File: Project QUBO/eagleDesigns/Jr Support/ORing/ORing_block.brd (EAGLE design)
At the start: 152.4 x 101.6 mm, 87 parts

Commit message: 
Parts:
- moved U$15 268.1 mm to (38.9, 88.2), turned to 270 degrees
- moved U$14 260.7 mm to (13.8, 83.4)
- moved U$5 256.3 mm to (22.3, 87.3), turned to 180 degrees
- moved R38 253.3 mm to (21.9, 84.6)
- moved R37 251.2 mm to (21.9, 82.3)
- moved C3 251.2 mm to (27.3, 82.7), turned to 90 degrees
- moved BATT1_IN 228.9 mm to (20.6, 94.5)
- moved U$20 198.5 mm to (88.5, 87.7), turned to 270 degrees
- moved U$19 180.4 mm to (60.8, 83.8)
- moved R35 174.2 mm to (75.5, 87.2), turned to 180 degrees
- moved R33 174.1 mm to (101.1, 129.5)
- moved C20 173.5 mm to (75.7, 83.5)
- moved U$13 171.6 mm to (70.0, 87.2), turned to 180 degrees
- moved LED7 171.4 mm to (98.2, 133.7), turned to 180 degrees
- moved R36 171.3 mm to (69.9, 84.3)
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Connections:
- removed net GND1: LED8.P$2
- removed net V_BATT3: R34.2
- net GND: now also LED8.P$2
- net V_BATT1: now also R34.2
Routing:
- net GND: track 15.0 -> 80.2 mm
- net V_BATT2: track 0.00 -> 61.6 mm, vias 0 -> 2
- net V_BATT: track 15.4 -> 51.1 mm, vias 0 -> 2
- net N$10: track 0.00 -> 31.5 mm, vias 0 -> 2
- net N$8: track 0.00 -> 30.6 mm, vias 0 -> 2
- net N$36: track 0.00 -> 24.5 mm
- net N$35: track 0.00 -> 23.9 mm
- net N$1: track 0.00 -> 23.3 mm, vias 0 -> 2
- net N$41: track 0.00 -> 23.0 mm, vias 0 -> 2
- net N$38: track 0.00 -> 20.2 mm
- net N$45: track 0.00 -> 20.2 mm
- net N$40: track 0.00 -> 20.0 mm
- net N$28: track 0.00 -> 18.9 mm, vias 0 -> 2
- net N$15: track 0.00 -> 17.8 mm
- net N$3: track 0.00 -> 13.2 mm
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- added copper zone on layer 1, net N$38

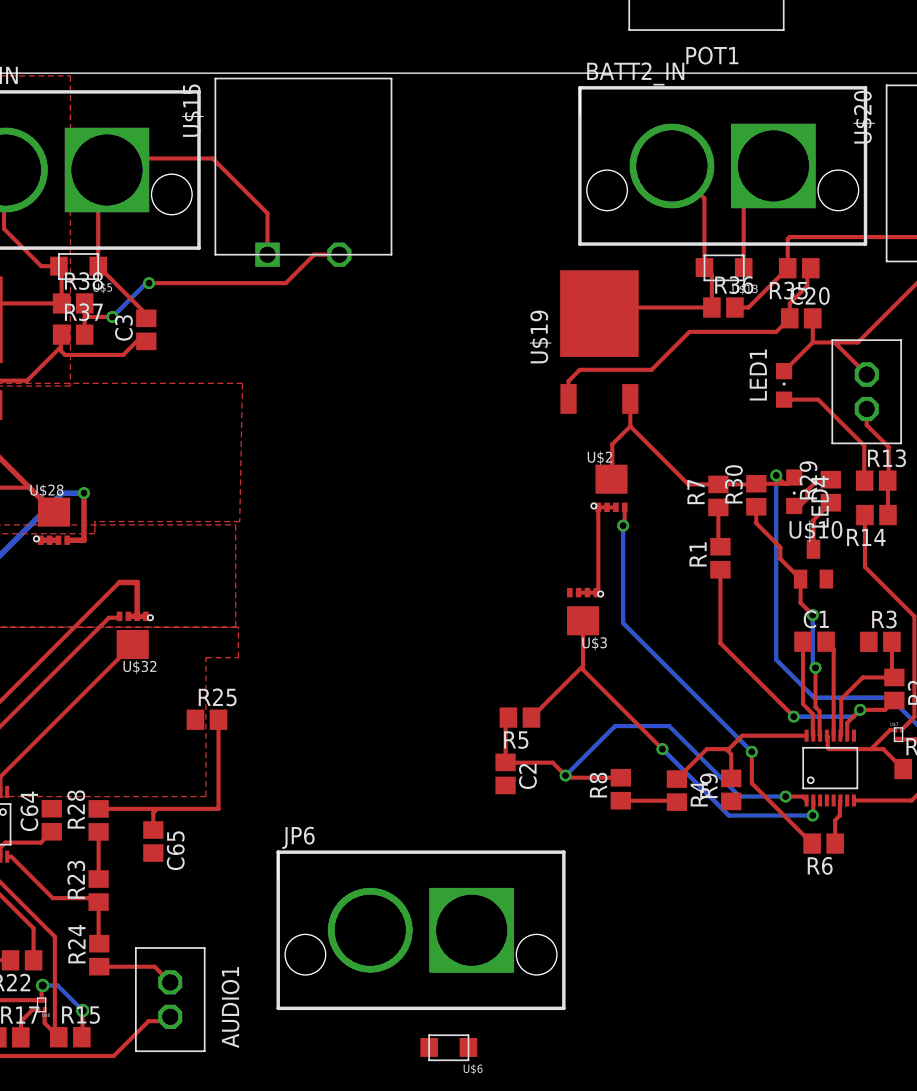
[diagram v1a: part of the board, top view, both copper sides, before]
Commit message: 
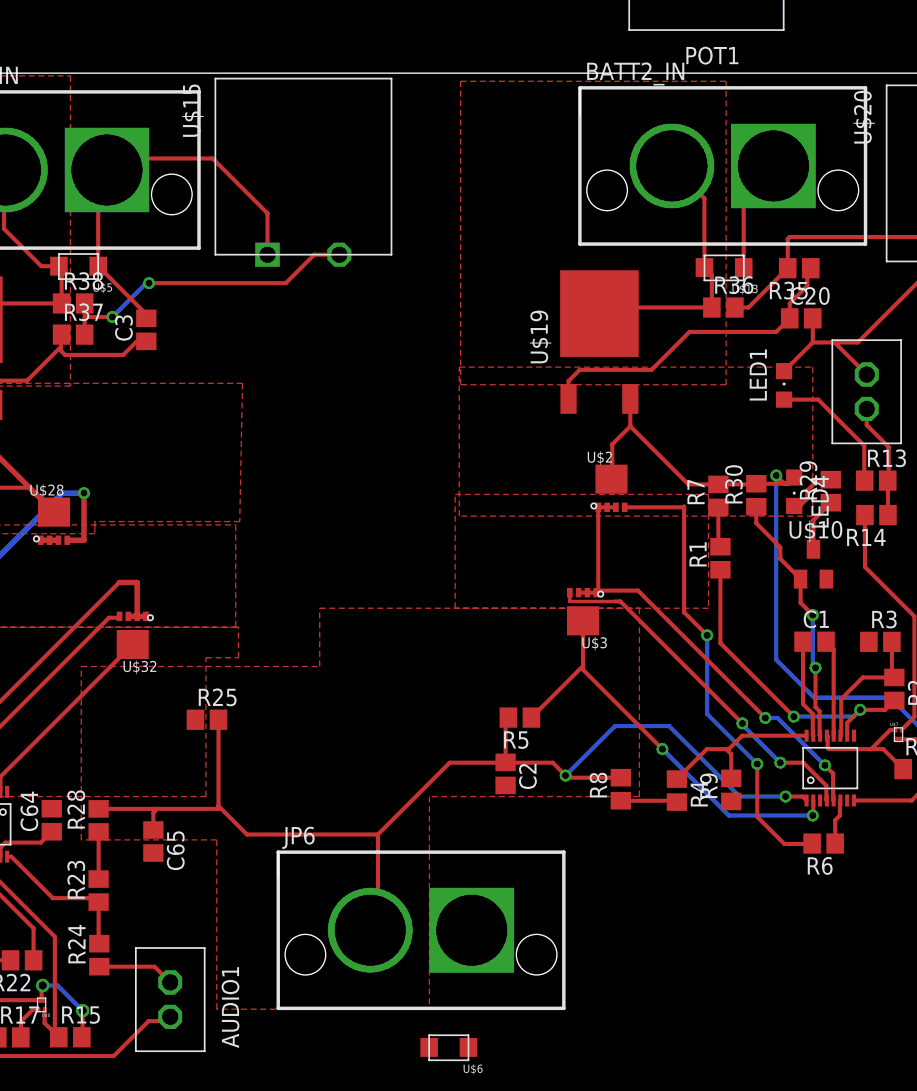
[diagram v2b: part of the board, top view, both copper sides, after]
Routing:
- net V_BATT: track 51.1 -> 82.6 mm
- net N$11: track 0.00 -> 26.4 mm, vias 0 -> 2
- net N$9: track 8.96 -> 33.9 mm, vias 0 -> 2
- net N$8: track 30.6 -> 34.4 mm
- added copper zone on layer 1, net N$45
- added copper zone on layer 1, net N$9
- added copper zone on layer 1, net V_BATT
- added copper zone on layer 1, net V_BATT2
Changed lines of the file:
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@@
 <contactref element="JP6" pad="P$1"/>
 <contactref element="U$6" pad="P$2"/>
-<wire x1="32.63" y1="53.87" x2="32.63" y2="47.29" width="0.3048" layer="1"/>
+<wire x1="32.63" y1="47.5" x2="32.63" y2="53.87" width="0.3048" layer="1"/>
+<wire x1="32.63" y1="47.5" x2="32.63" y2="47.29" width="0.3048" layer="1"/>
 <wire x1="28.1" y1="47.29" x2="32.63" y2="47.29" width="0.3048" layer="1"/>
 <wire x1="28.1" y1="47.29" x2="23.78" y2="47.29" width="0.3048" layer="1"/>
@@
 <wire x1="61.9" y1="53.4" x2="58.25" y2="49.75" width="0.3048" layer="16"/>
 <via x="58.25" y="49.75" extent="1-16" drill="0.5"/>
-<wire x1="43.8335" y1="38.33" x2="53.84" y2="50.7" width="0" layer="19" extent="1-1"/>
-<wire x1="48.18" y1="29.68" x2="43.8335" y2="38.33" width="0" layer="19" extent="1-1"/>
-<wire x1="32.63" y1="47.29" x2="43.8335" y2="38.33" width="0" layer="19" extent="1-1"/>
+<wire x1="53.84" y1="50.7" x2="49.7" y2="50.7" width="0.3048" layer="1"/>
+<wire x1="49.7" y1="50.7" x2="44.4" y2="45.4" width="0.3048" layer="1"/>
+<wire x1="44.4" y1="45.4" x2="44.4" y2="38.8965" width="0.3048" layer="1"/>
+<wire x1="44.4" y1="38.8965" x2="43.8335" y2="38.33" width="0.3048" layer="1"/>
+<wire x1="44.4" y1="45.4" x2="34.73" y2="45.4" width="0.3048" layer="1"/>
+<wire x1="34.73" y1="45.4" x2="32.63" y2="47.5" width="0.3048" layer="1"/>
+<polygon width="0.3048" layer="1" rank="4">
+<vertex x="31.7" y="57.8"/>
+<vertex x="40.1" y="57.8"/>
+<vertex x="40.1" y="62.1"/>
+<vertex x="63.7" y="62.1"/>
+<vertex x="63.7" y="48.2"/>
+<vertex x="48.2" y="48.2"/>
+<vertex x="48.2" y="32.5"/>
+<vertex x="32.5" y="32.5"/>
+<vertex x="32.5" y="45"/>
+<vertex x="22.5" y="45"/>
+<vertex x="22.5" y="57.8"/>
+</polygon>
+<wire x1="43.8335" y1="38.33" x2="48.18" y2="29.68" width="0" layer="19" extent="1-1"/>
 <wire x1="17.03" y1="48.54" x2="23.78" y2="47.29" width="0" layer="19" extent="1-1"/>
 </signal>
@@
 <contactref element="R6" pad="2"/>
 <contactref element="U$2" pad="GATE"/>
-<wire x1="76.45" y1="44.73" x2="72" y2="49.18" width="0.3048" layer="1"/>
-<wire x1="72" y1="49.18" x2="72" y2="51.5" width="0.3048" layer="1"/>
-<via x="72" y="51.5" extent="1-16" drill="0.5"/>
-<wire x1="72" y1="51.5" x2="62.5" y2="61" width="0.3048" layer="16"/>
-<wire x1="62.5" y1="61" x2="62.5" y2="68.2" width="0.3048" layer="16"/>
-<via x="62.5" y="68.2" extent="1-16" drill="0.5"/>
-<wire x1="62.5" y1="68.2" x2="62.615" y2="68.315" width="0.3048" layer="1"/>
-<wire x1="62.615" y1="68.315" x2="62.615" y2="69.55" width="0.3048" layer="1"/>
+<wire x1="62.615" y1="69.55" x2="66.95" y2="69.55" width="0.3048" layer="1"/>
+<wire x1="66.95" y1="69.55" x2="67" y2="69.6" width="0.3048" layer="1"/>
+<wire x1="67" y1="69.6" x2="67" y2="61.8" width="0.3048" layer="1"/>
+<wire x1="67" y1="61.8" x2="68.7" y2="60.1" width="0.3048" layer="1"/>
+<via x="68.7" y="60.1" extent="1-16" drill="0.5"/>
+<wire x1="68.7" y1="60.1" x2="68.7" y2="54.3" width="0.3048" layer="16"/>
+<wire x1="68.7" y1="54.3" x2="72.4" y2="50.6" width="0.3048" layer="16"/>
+<via x="72.4" y="50.6" extent="1-16" drill="0.5"/>
+<wire x1="72.4" y1="50.6" x2="72.4" y2="46.7" width="0.3048" layer="1"/>
+<wire x1="72.4" y1="46.7" x2="74.4" y2="44.7" width="0.3048" layer="1"/>
+<wire x1="74.4" y1="44.7" x2="76.42" y2="44.7" width="0.3048" layer="1"/>
+<wire x1="76.42" y1="44.7" x2="76.45" y2="44.73" width="0.3048" layer="1"/>
 </signal>
 <signal name="N$9">
@@
 <wire x1="59.865" y1="63.25" x2="60.515" y2="63.25" width="0.3048" layer="1"/>
 <wire x1="59.215" y1="63.25" x2="59.865" y2="63.25" width="0.3048" layer="1"/>
-<wire x1="60.665" y1="63.4" x2="78.04" y2="47.91" width="0" layer="19" extent="1-1"/>
+<wire x1="60.665" y1="63.4" x2="63.6" y2="63.4" width="0.3048" layer="1"/>
+<wire x1="63.6" y1="63.4" x2="73" y2="54" width="0.3048" layer="1"/>
+<via x="73" y="54" extent="1-16" drill="0.5"/>
+<wire x1="73" y1="54" x2="73.9" y2="54" width="0.3048" layer="16"/>
+<wire x1="73.9" y1="54" x2="77.4" y2="50.5" width="0.3048" layer="16"/>
+<via x="77.4" y="50.5" extent="1-16" drill="0.5"/>
+<wire x1="77.4" y1="50.5" x2="78" y2="49.9" width="0.3048" layer="1"/>
+<wire x1="78" y1="49.9" x2="78" y2="47.95" width="0.3048" layer="1"/>
+<wire x1="78" y1="47.95" x2="78.04" y2="47.91" width="0.3048" layer="1"/>
+<polygon width="0.3048" layer="1">
+<vertex x="50.1" y="70.5"/>
+<vertex x="68.8" y="70.5"/>
+<vertex x="68.8" y="62.1"/>
+<vertex x="50.1" y="62.1"/>
+</polygon>
 </signal>
 <signal name="N$10">
@@
 <contactref element="U$1" pad="DGATE"/>
 <contactref element="U$3" pad="GATE"/>
-<wire x1="58.565" y1="63.25" x2="77.54" y2="47.91" width="0" layer="19" extent="1-1"/>
+<wire x1="58.565" y1="63.25" x2="58.565" y2="62.6" width="0.254" layer="1"/>
+<wire x1="58.565" y1="62.6" x2="61.9" y2="62.6" width="0.254" layer="1"/>
+<wire x1="61.9" y1="62.6" x2="62.3" y2="62.6" width="0.3048" layer="1"/>
+<wire x1="62.3" y1="62.6" x2="71.3" y2="53.6" width="0.3048" layer="1"/>
+<via x="71.3" y="53.6" extent="1-16" drill="0.5"/>
+<wire x1="71.3" y1="53.6" x2="71.3" y2="53.5" width="0.3048" layer="16"/>
+<wire x1="71.3" y1="53.5" x2="74.1" y2="50.7" width="0.3048" layer="16"/>
+<via x="74.1" y="50.7" extent="1-16" drill="0.5"/>
+<wire x1="74.1" y1="50.7" x2="75.8" y2="50.7" width="0.3048" layer="1"/>
+<wire x1="75.8" y1="50.7" x2="77.5" y2="49" width="0.3048" layer="1"/>
+<wire x1="77.5" y1="49" x2="77.5" y2="47.95" width="0.3048" layer="1"/>
+<wire x1="77.5" y1="47.95" x2="77.54" y2="47.91" width="0.3048" layer="1"/>
 </signal>
 <signal name="V_BATT2">
@@
 <wire x1="85.3" y1="52" x2="84.9" y2="51.6" width="0.3048" layer="1"/>
 <wire x1="76.6" y1="55.5" x2="82.2" y2="55.5" width="0.3048" layer="16"/>
+<polygon width="0.3048" layer="1" rank="2">
+<vertex x="50.4" y="79.9"/>
+<vertex x="76.5" y="79.9"/>
+<vertex x="76.5" y="68.9"/>
+<vertex x="50.4" y="68.9"/>
+</polygon>
 <wire x1="105.23" y1="123.94" x2="101.95" y2="129.5" width="0" layer="19" extent="1-1"/>
 <wire x1="95.9" y1="126.82" x2="101.95" y2="129.5" width="0" layer="19" extent="1-1"/>
@@
 <wire x1="69.05" y1="84.3" x2="61.2" y2="84.3" width="0.3048" layer="1"/>
 <wire x1="61.2" y1="84.3" x2="60.75" y2="83.85" width="0.3048" layer="1"/>
+<polygon width="0.3048" layer="1">
+<vertex x="50.5" y="101"/>
+<vertex x="70.1" y="101"/>
+<vertex x="70.1" y="78.6"/>
+<vertex x="50.5" y="78.6"/>
+</polygon>
 </signal>
 <signal name="N$35">

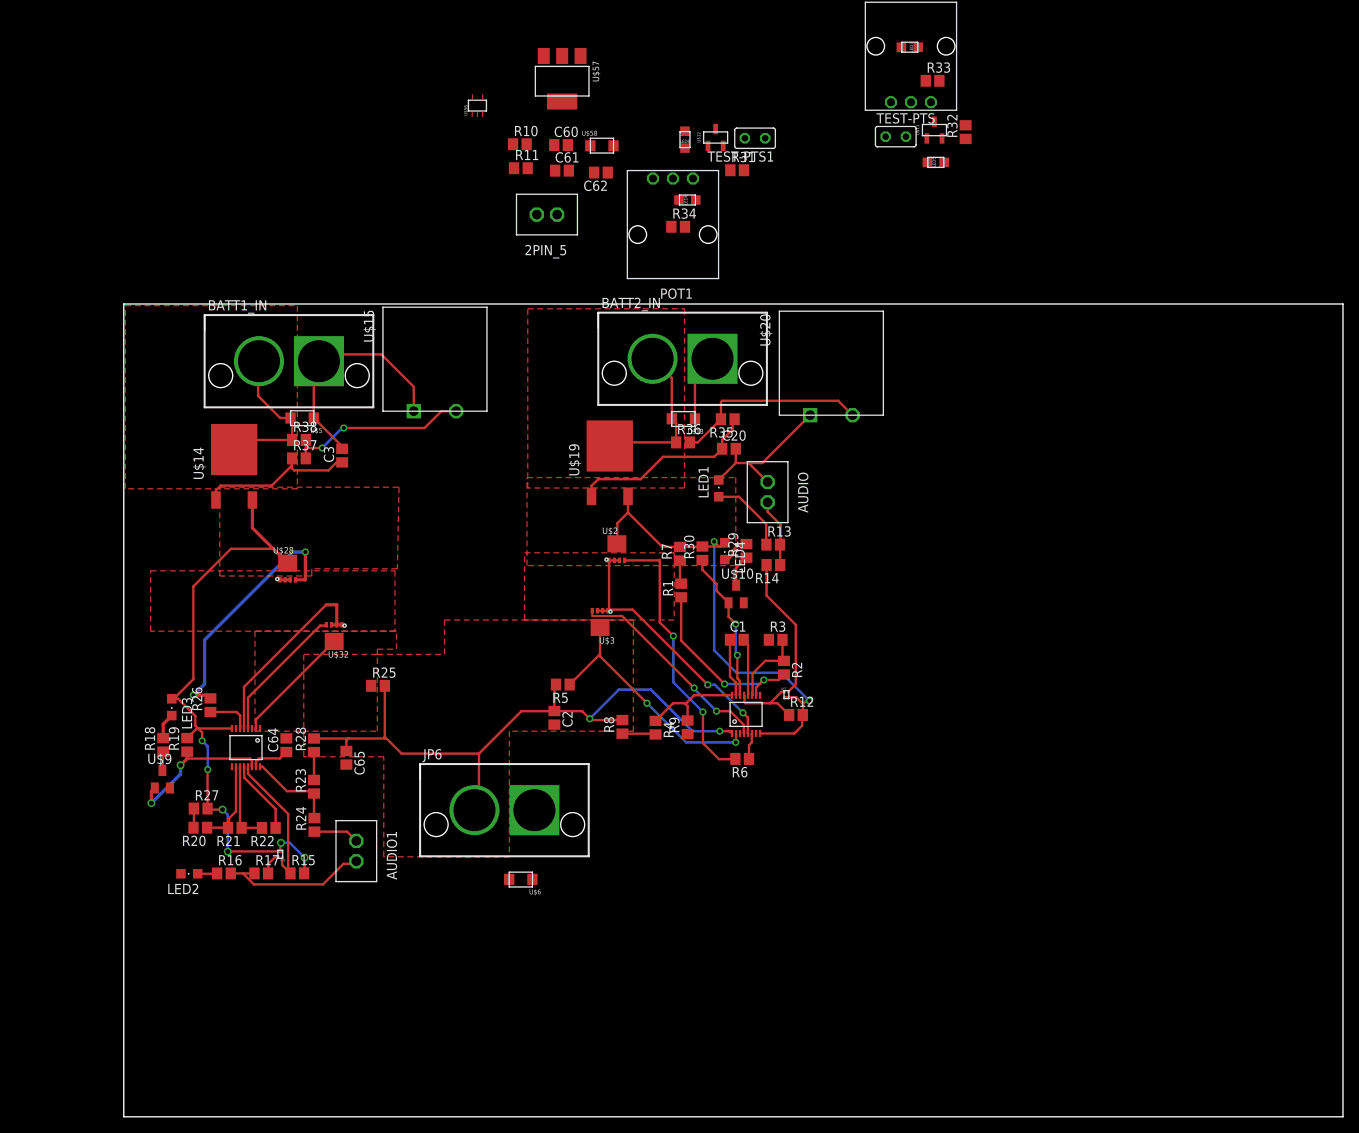
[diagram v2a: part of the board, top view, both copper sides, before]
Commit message: 
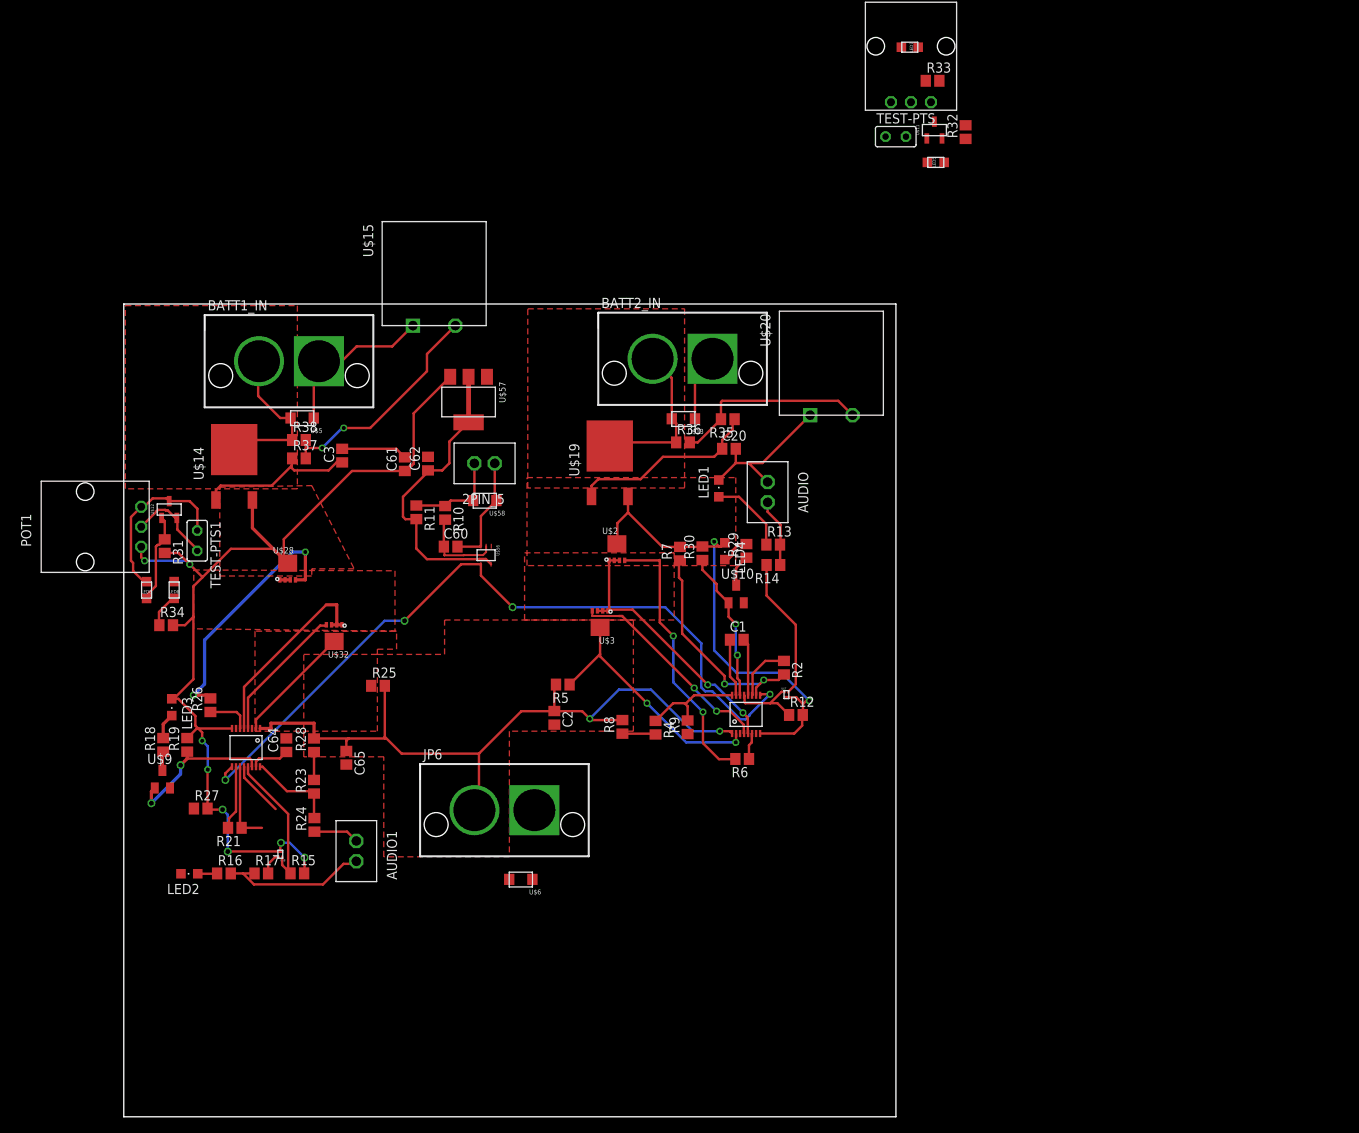
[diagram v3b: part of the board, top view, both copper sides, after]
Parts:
- removed R1, R20, R22, R3: 10k, resistor:R0805
- R2: value 12k -> 20.8k
- moved LED6 87.7 mm to (2.85, 65.8)
- moved TEST-PTS1 86.0 mm to (9.18, 72.0), turned to 270 degrees
- moved R31 85.6 mm to (5.12, 71.3), turned to 270 degrees
- moved U$12 82.6 mm to (5.68, 75.9)
- moved R34 81.1 mm to (5.30, 61.5)
- moved LED8 80.6 mm to (6.30, 65.8), turned to 90 degrees
- moved POT1 79.5 mm to (2.18, 73.8), turned to 90 degrees
- moved U$56 56.2 mm to (45.3, 70.2), turned to 180 degrees
- moved C60 52.1 mm to (40.9, 71.3)
- moved R10 47.0 mm to (40.2, 75.5), turned to 270 degrees
- moved U$58 46.7 mm to (45.1, 77.0), turned to 180 degrees
- moved R11 45.0 mm to (36.6, 75.6), turned to 270 degrees
- moved C62 42.3 mm to (38.0, 81.7), turned to 90 degrees
- moved U$57 41.8 mm to (43.1, 89.3)
- moved C61 41.6 mm to (35.1, 81.6), turned to 90 degrees
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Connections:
- removed net N$2: R2.1, R3.2, U$1.OV
- removed net N$47: R21.1, R22.2, U$27.OV
- removed net N$5: R1.2, R7.1
- removed net N$51: R20.2, R27.1
- net GND: now also R2.1, R21.1, U$1.OV, U$27.OV; no longer R22.1, R3.1
- net N$1: now also R7.1; no longer R1.1
- net N$39: now also R27.1; no longer R20.1
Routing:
- net N$14: track 0.00 -> 96.0 mm, vias 0 -> 4
- net V_BATT1: track 82.1 -> 134.9 mm, vias 6 -> 8
- net N$13: track 0.00 -> 37.6 mm
- net GND: track 80.2 -> 116.9 mm
- net N$48: track 0.00 -> 14.2 mm
- net N$12: track 0.00 -> 12.1 mm
- net N$32: track 0.00 -> 11.3 mm
- net N$31: track 0.00 -> 10.9 mm
- net N$49: track 0.00 -> 10.7 mm
- net N$47: track 10.3 -> 0.00 mm
- net N$2: track 10.0 -> 0.00 mm
- net V_BATT: track 82.6 -> 92.0 mm
- net N$41: track 23.0 -> 28.6 mm
- net N$1: track 23.3 -> 28.1 mm
- net N$34: track 0.00 -> 4.27 mm
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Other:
- board size 152.4 x 101.6 mm -> 96.5 x 101.6 mm
